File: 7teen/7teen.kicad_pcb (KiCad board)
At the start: 2 copper layers, 34 parts, among them U0 SeeeduinoXIAO

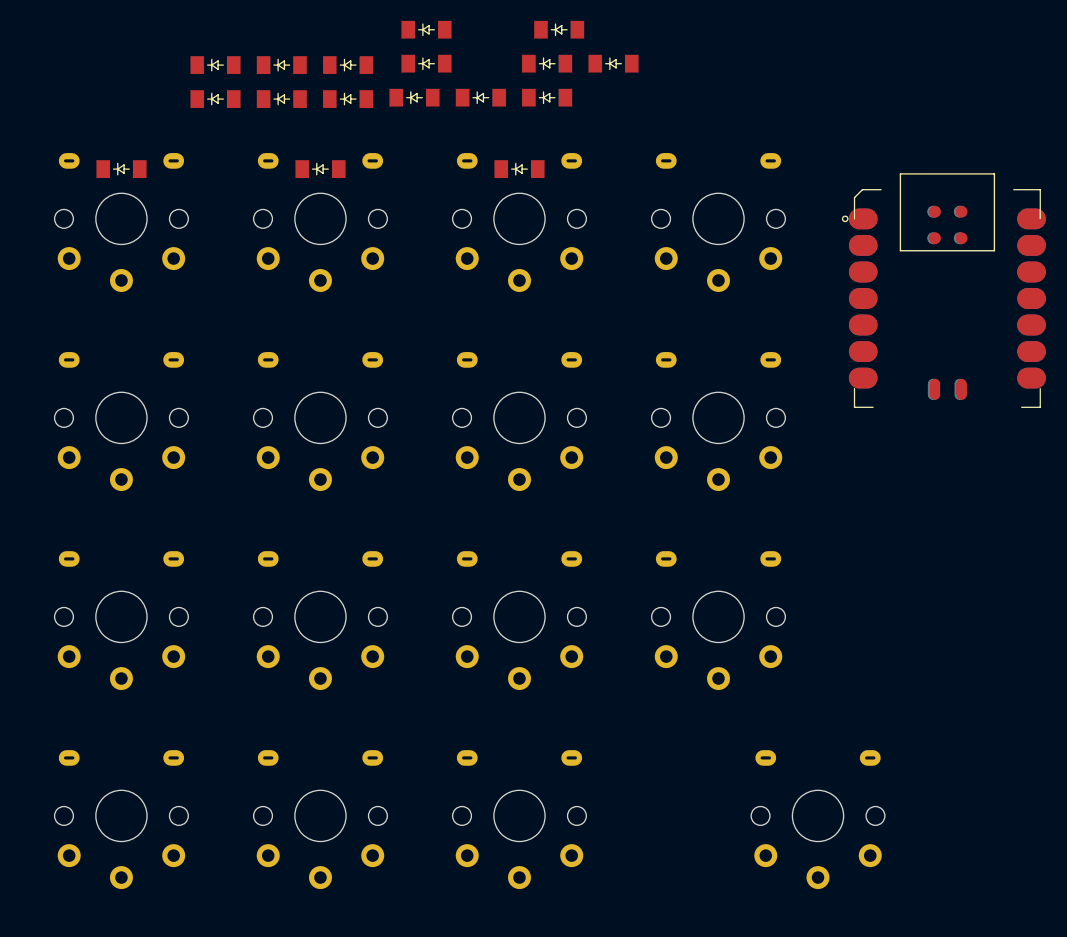
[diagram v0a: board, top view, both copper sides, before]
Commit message: [keyboard] 7teen: pcb development
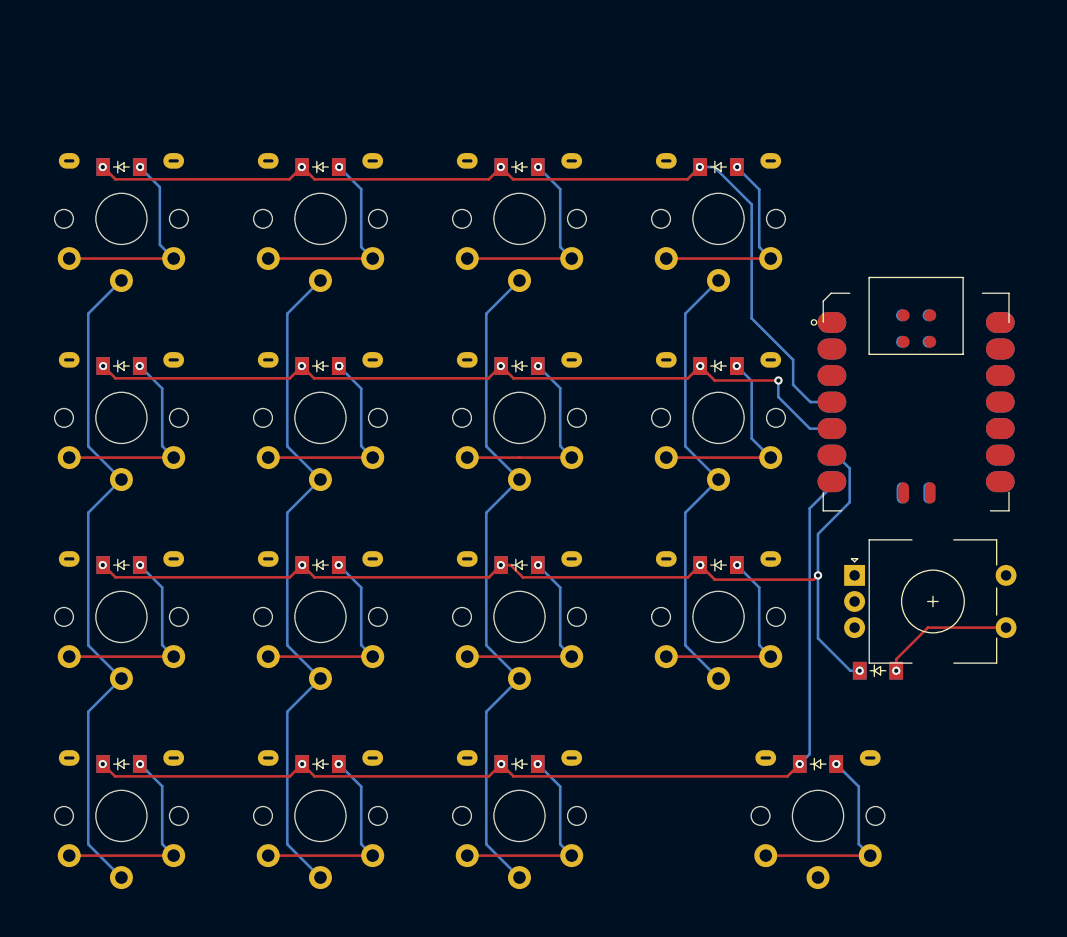
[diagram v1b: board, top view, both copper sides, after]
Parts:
- added REF**: layout_7teen, keeblib:layout_7teen, F.Cu at (66.7, 181.0)
- added SwC4: Rotary_Encoder_Switch, keebio:RotaryEncoder_EC11, F.Cu at (144.4, 160.5)
- moved D_D4 88.3 mm to (133.4, 176.0)
- moved D_C4 79.1 mm to (139.1, 167.1)
- moved D_D2 70.7 mm to (104.8, 176.0)
- moved D_D1 67.0 mm to (85.7, 176.0)
- moved D_D0 64.3 mm to (66.7, 176.0)
- moved D_C3 57.0 mm to (123.8, 157.0)
- moved D_C0 56.2 mm to (66.7, 157.0)
- moved D_C1 55.6 mm to (85.7, 157.0)
- moved D_C2 52.0 mm to (104.8, 157.0)
- moved D_B0 48.2 mm to (66.7, 137.9)
- moved D_B3 38.8 mm to (123.8, 137.9)
- moved D_B1 36.2 mm to (85.7, 137.9)
- moved D_B2 26.0 mm to (104.8, 137.9)
- moved D_A3 20.1 mm to (123.8, 118.9)
- moved U0 10.4 mm to (135.1, 133.7)
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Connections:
- D_C4 pad 2: (no net) -> Net-(D_C4-Pad2)
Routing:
- net rowD: track 0.00 -> 98.1 mm, vias 0 -> 4
- net rowC: track 0.00 -> 96.7 mm, vias 0 -> 6
- net rowA: track 0.00 -> 90.2 mm, vias 0 -> 4
- net rowB: track 0.00 -> 76.5 mm, vias 0 -> 5
- net col0: track 0.00 -> 65.0 mm
- net col1: track 0.00 -> 65.0 mm
- net col2: track 0.00 -> 65.0 mm
- net col3: track 0.00 -> 43.4 mm
- net Net-(D_A0-Pad2): track 0.00 -> 20.1 mm, vias 0 -> 1
- net Net-(D_B0-Pad2): track 0.00 -> 20.1 mm, vias 0 -> 1
- net Net-(D_A3-Pad2): track 0.00 -> 20.1 mm, vias 0 -> 1
- net Net-(D_B1-Pad2): track 0.00 -> 20.1 mm, vias 0 -> 2
- net Net-(D_C0-Pad2): track 0.00 -> 20.1 mm, vias 0 -> 1
- net Net-(D_B3-Pad2): track 0.00 -> 20.1 mm, vias 0 -> 1
- net Net-(D_C1-Pad2): track 0.00 -> 20.1 mm, vias 0 -> 1
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
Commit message: [keyboard] 7teen: pcb development
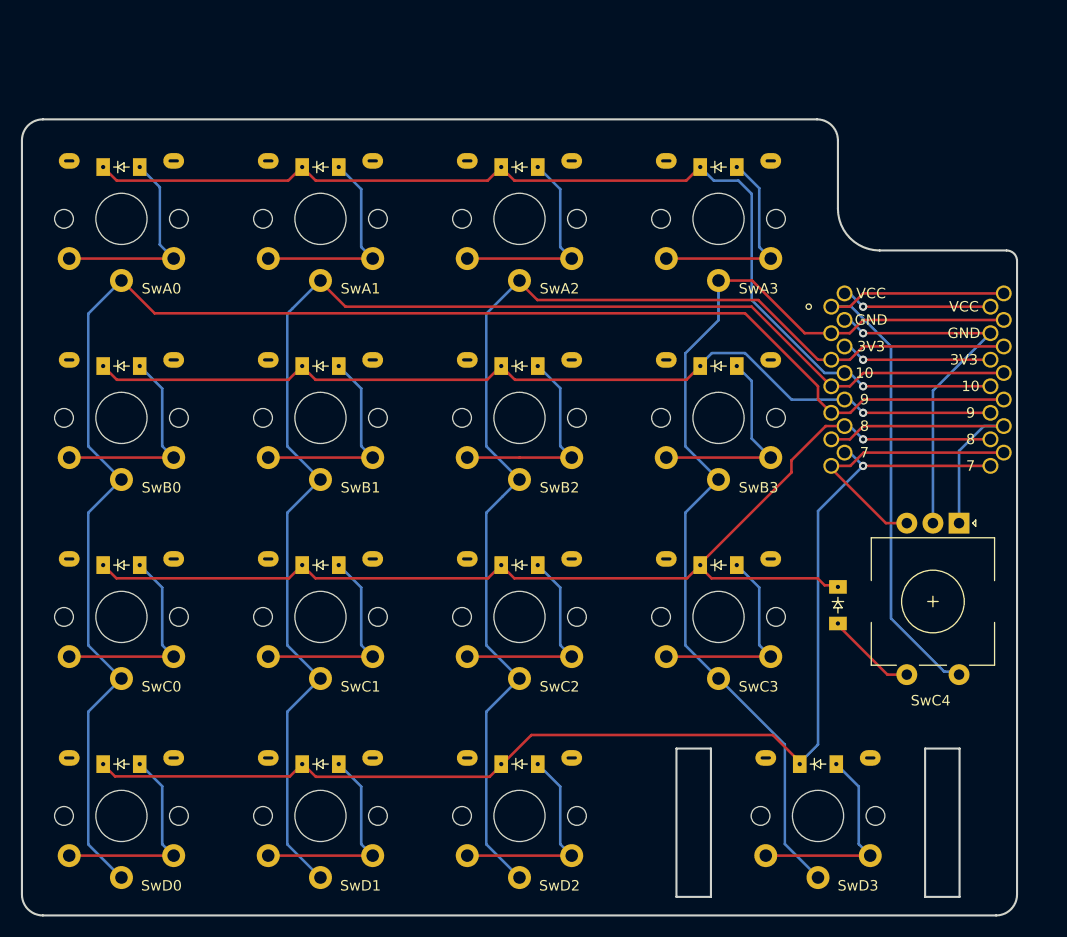
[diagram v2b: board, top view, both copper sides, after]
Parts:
- added REF**: edgecuts_7teen, keeblib:edgecuts_7teen, F.Cu at (57.1, 190.5)
- U0: footprint keeblib:Seeeduino_XIAO_dual -> keeblib:Seeeduino_XIAO_dual_tht
- moved D_C4 7.35 mm to (135.3, 160.8), turned to 270 degrees
- moved U0 1.59 mm to (134.6, 132.2)
- turned SwC4 to 270 degrees
- renumbered D_D4 to D_D3, SwD4 to SwD3
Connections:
- SwD3 pad 2: col4 -> col3
- U0 pad 1: col0 -> col4
- U0 pad 2: col1 -> col3
- U0 pad 4: col3 -> col1
- U0 pad 5: col4 -> col0
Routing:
- net col0: track 65.0 -> 156.0 mm
- net col1: track 65.0 -> 135.3 mm
- net col4: track 0.00 -> 58.8 mm
- net col3: track 43.4 -> 96.3 mm
- net col2: track 65.0 -> 115.2 mm
- net GND: track 0.00 -> 34.5 mm, vias 0 -> 1
- net encA: track 0.00 -> 29.2 mm
- net encB: track 0.00 -> 26.6 mm
- net rowD: track 98.1 -> 116.6 mm, vias 4 -> 1
- net Net-(U0-Pad14): track 0.00 -> 14.5 mm, vias 0 -> 1
- net Net-(U0-Pad12): track 0.00 -> 14.5 mm, vias 0 -> 1
- net rowB: track 76.5 -> 91.0 mm, vias 5 -> 1
- net rowA: track 90.2 -> 102.3 mm, vias 4 -> 1
- net rowC: track 96.7 -> 108.6 mm, vias 6 -> 1
- net Net-(D_C4-Pad2): track 12.9 -> 8.56 mm, vias 1 -> 0
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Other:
- board outline added: 95.2 x 76.2 mm
- board text added: "SwC4"

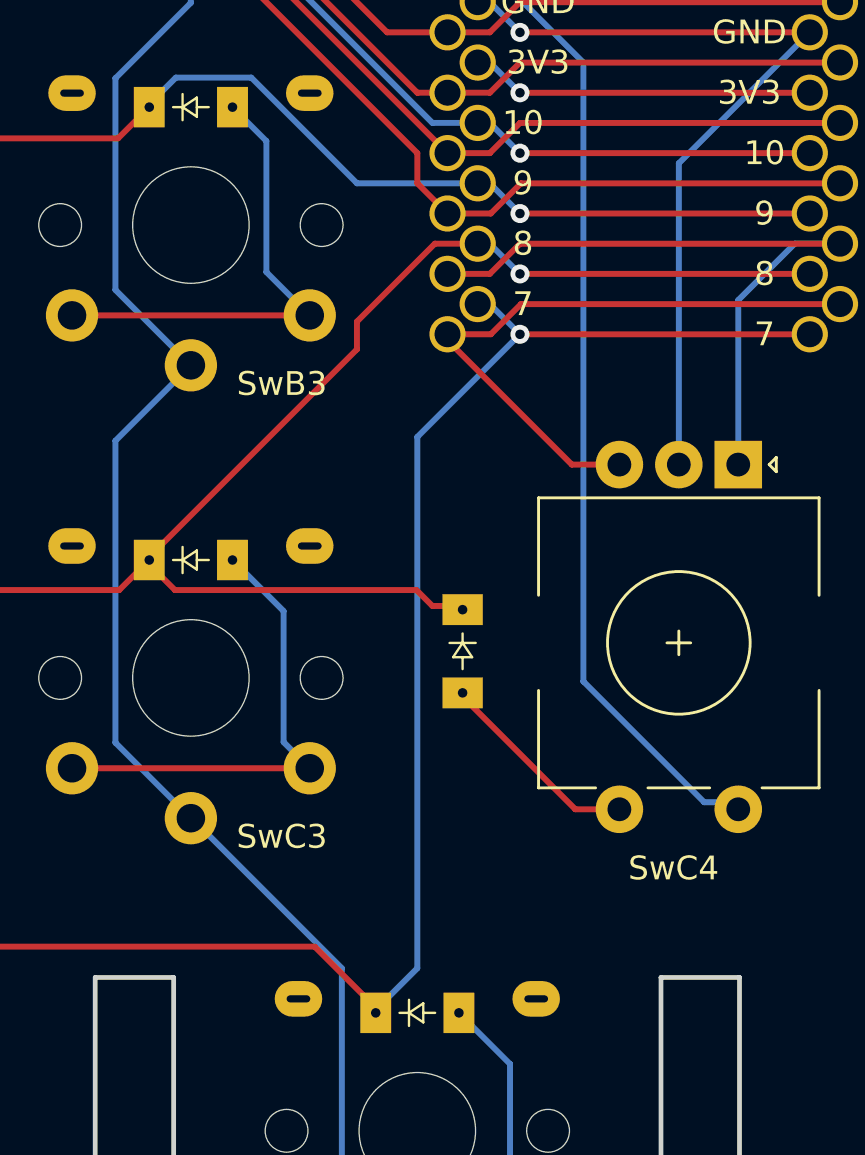
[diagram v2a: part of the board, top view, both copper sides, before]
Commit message: [keyboard] 7teen: pcb development
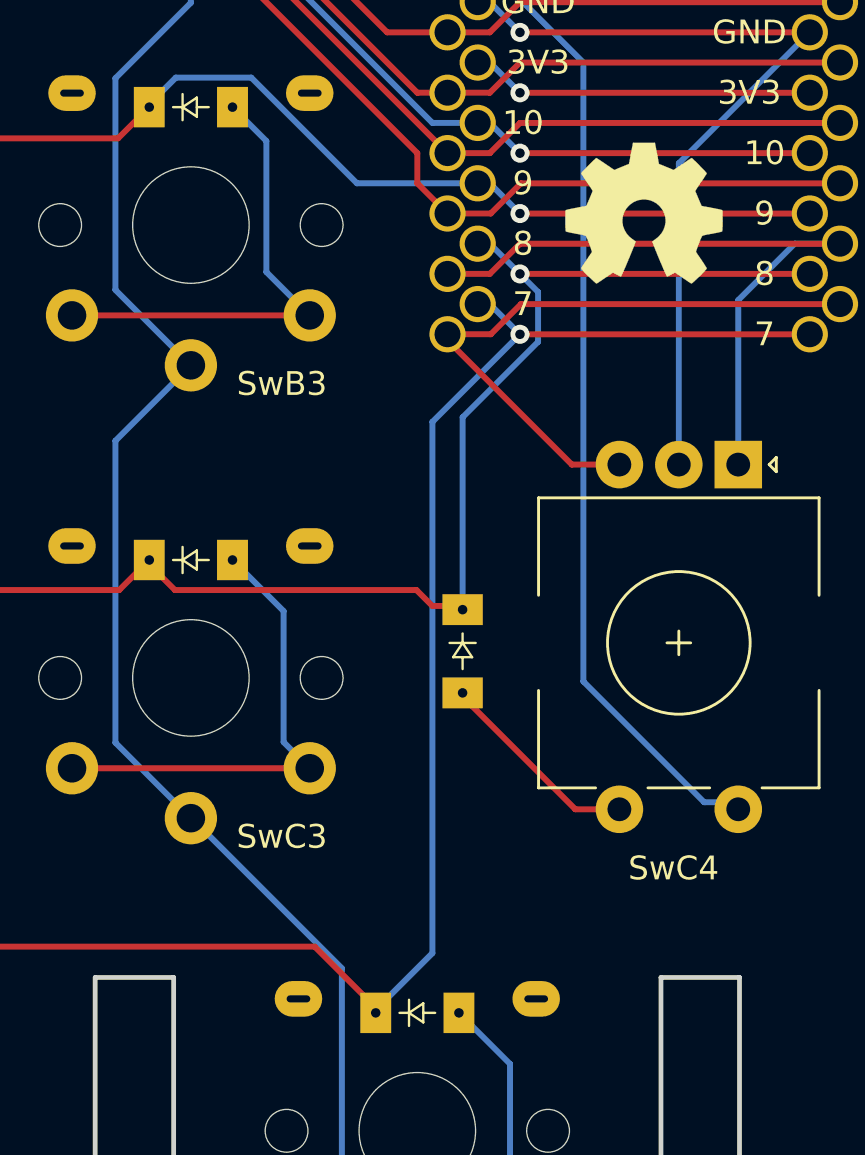
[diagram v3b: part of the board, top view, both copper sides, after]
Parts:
- added REF**: OSHW-Symbol_6.7x6mm_SilkScreen, Symbol:OSHW-Symbol_6.7x6mm_SilkScreen, B.Cu at (142.9, 142.4)
- added REF**: OSHW-Symbol_6.7x6mm_SilkScreen, Symbol:OSHW-Symbol_6.7x6mm_SilkScreen, F.Cu at (142.9, 142.4)
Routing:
- net rowC: track 108.6 -> 104.0 mm
